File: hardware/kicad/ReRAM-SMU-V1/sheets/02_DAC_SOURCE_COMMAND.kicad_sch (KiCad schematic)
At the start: 38 parts, among them U1 AD5764CSUZ PRIMARY 5V ref 20V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, U2 ADA4522-1 VCSRC conditioning 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, U3 ADA4522-1 VCSNK conditioning 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

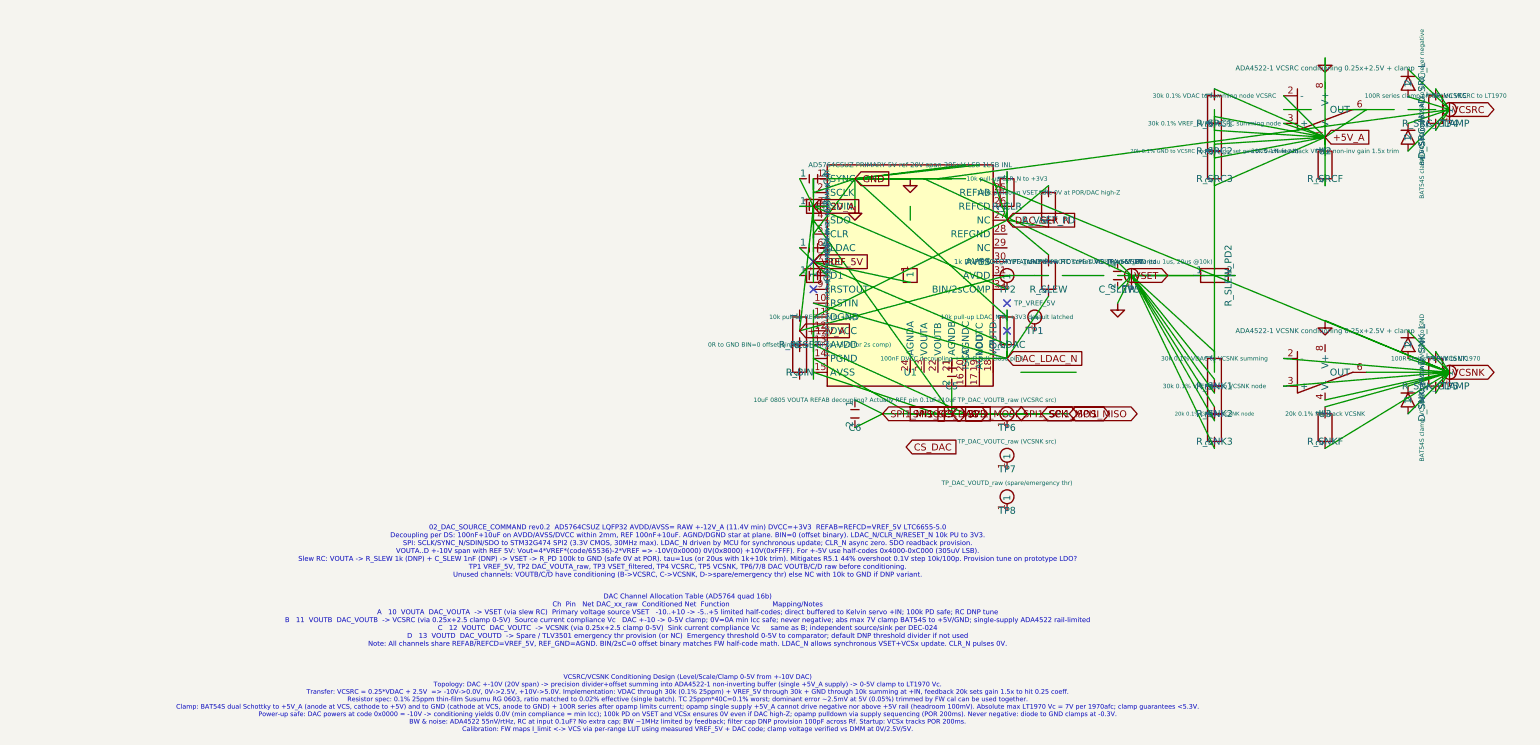
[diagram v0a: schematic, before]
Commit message: style(kicad): re-serialize 01-06 + root to KiCad 9.0 schema 20250114 (formatting only)
- (version 20241014)->(version 20250114) + generator_version 10.0->9.0 on all 10 sch files including root + 01-04 verified via git diff
- lib_symbols block pretty-print expansion: property/symbol multi-line with explicit hide/exclude/effects font, no wire/symbol/net deletion
- 8 files: ReRAM-SMU-V1.kicad_pro (453+9-), ReRAM-SMU-V1.kicad_sch (806+53-), 01_POWER (5724+411-), 02_DAC (5816+436-), 03_OUTPUT (4308+276-), 04_KELVIN (3720+270-), 05_CURRENT_RANGES (375+217-), 06_ADC (492+452-); total 21694+2124-
- 07/08/09 excluded (already restored 184/236/156 lines, verified not truncated; no re-serialization needed)
- Functional audit: no net/junction/wire loss, netlist continuity preserved, ERC 124 headless (ca7eac3) unchanged by re-serialization
- Verified: wc -l 01 5739,02 5831,03 4322,04 3735,05 388,06 507,07 184,08 236,09 156
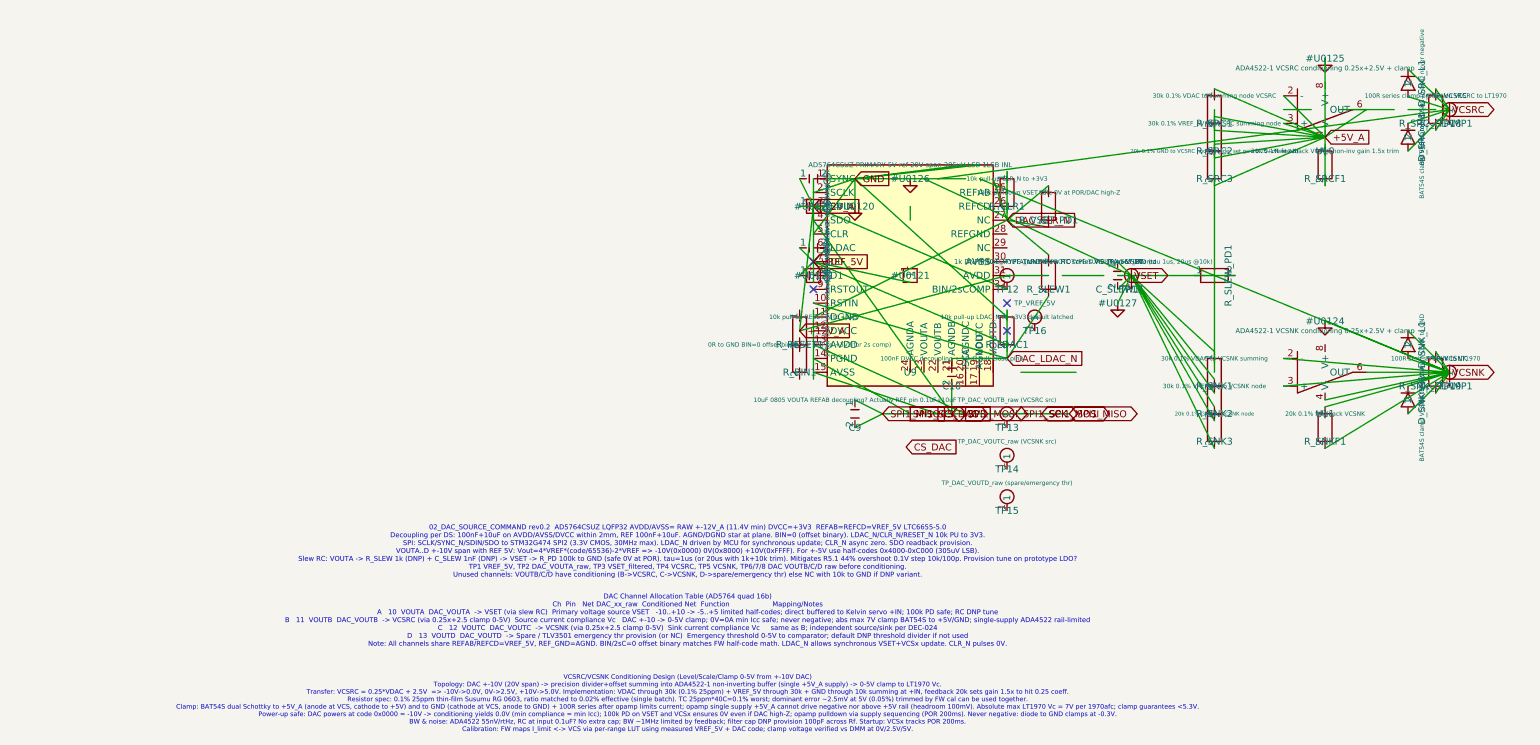
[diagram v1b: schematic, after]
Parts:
- added D_SRC_H1: BAT54S clamp VCSRC to +5V_A, Diode_SMD:D_SOT-23, symbol Device:D_Schottky
- R_RESET1: renamed from D_SRC_H; value BAT54S clamp VCSRC to +5V_A -> 10k pull-up RESET_N to +3V3; footprint Diode_SMD:D_SOT-23 -> Resistor_SMD:R_0603_1608Metric; symbol Device:D_Schottky -> Device:R
- renumbered C5 to C10, C4 to C5, C3 to C6, C2 to C7, C1 to C8, C6 to C9, C_SLEW to C_SLEW1, D_SNK_H to D_SNK_H1, D_SNK_L to D_SNK_L1, D_SRC_L to D_SRC_L1, R_BIN to R_BIN1, R_CLR to R_CLR1, R_LDAC to R_LDAC1, R_SLEW to R_SLEW1, R_SLEW_PD2 to R_SLEW_PD1, R_SNKF to R_SNKF1, R_SNK_CLAMP to R_SNK_CLAMP1, R_SRCF to R_SRCF1, R_SRC_CLAMP to R_SRC_CLAMP1, R_VSET_PD to R_VSET_PD1, TP2 to TP12, TP6 to TP13, TP7 to TP14, TP8 to TP15, TP1 to TP16, TP3 to TP17, TP4 to TP18, TP5 to TP19, U2 to U10, U3 to U11, U1 to U9
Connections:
- net +12V_A: no longer C10.2, C5.2, C9.1, C9.2, U9.13 (AVDD), U9.14 (PGND), U9.15 (AVSS), U9.2 (SCLK), U9.4 (SDO), U9.5 (CLR), U9.6 (LDAC)
- net +5V_A: no longer R_SRCF1.1
- net DAC_CLR_N: no longer R_CLR1.2
- net DAC_LDAC_N: no longer R_LDAC1.2
- net VCSRC: now also D_SRC_H1.1, D_SRC_H1.2; no longer R_RESET1.1, R_RESET1.2
- net VSET: no longer R_SLEW_PD1.1
- new net +3V3: C10.2, C9.1, C9.2, U9.13 (AVDD), U9.14 (PGND), U9.15 (AVSS), U9.4 (SDO)
- new net GND: C5.2, U9.2 (SCLK), U9.5 (CLR)
